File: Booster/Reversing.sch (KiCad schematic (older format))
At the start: 21 parts

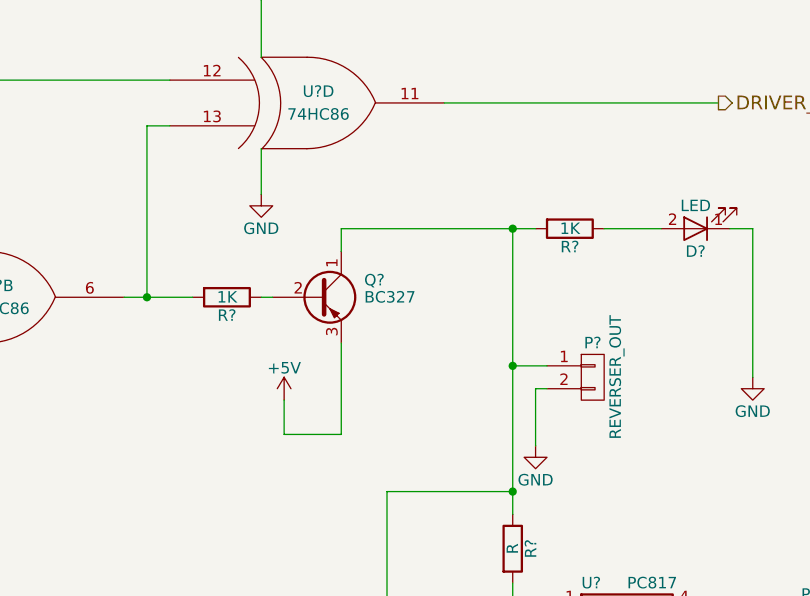
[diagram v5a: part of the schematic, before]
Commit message: Changed transistor driving reversing indicator LED to NPN to get it to light up when reversing, not light up when not reversing.
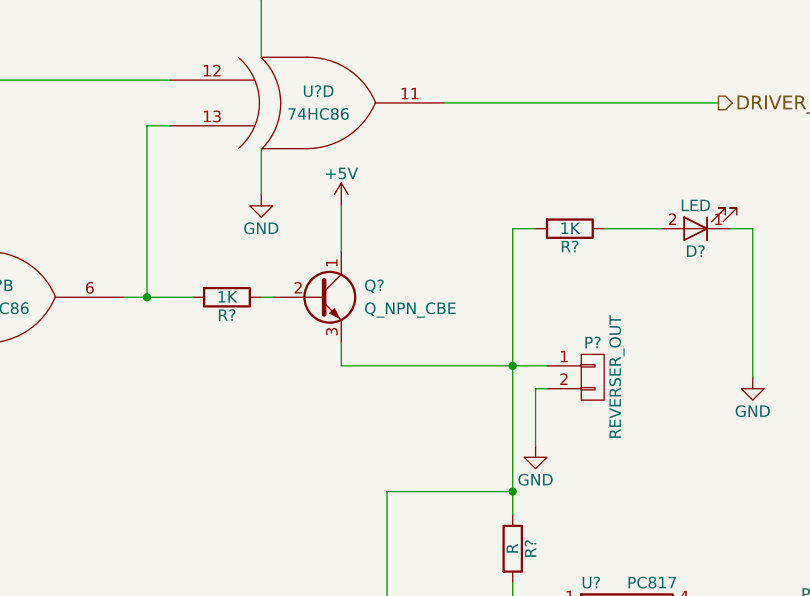
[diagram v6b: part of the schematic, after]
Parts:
- removed Q?: BC327, TO_SOT_Packages_THT:TO-92_Molded_Narrow, symbol BC327
- added Q?: Q_NPN_CBE, symbol Q_NPN_CBE
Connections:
- net +5V: now also Q?.1 (C)
- net at R?.1: now also Q?.2 (B)
- net at P?.1 (P1), R?.1, R?.1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: now also Q?.3 (E)
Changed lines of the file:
@@
 L +5V #PWR?
 U 1 1 5A08AC26
-P 5350 3900
-F 0 "#PWR?" H 5350 3750 50  0001 C CNN
-F 1 "+5V" H 5350 4040 50  0000 C CNN
-F 2 "" H 5350 3900 50  0000 C CNN
-F 3 "" H 5350 3900 50  0000 C CNN
-	1    5350 3900
+P 5600 3050
+F 0 "#PWR?" H 5600 2900 50  0001 C CNN
+F 1 "+5V" H 5600 3190 50  0000 C CNN
+F 2 "" H 5600 3050 50  0000 C CNN
+F 3 "" H 5600 3050 50  0000 C CNN
+	1    5600 3050
 	1    0    0    -1
 $EndComp
@@
 Wire Wire Line
 	6500 3850 6450 3850
-Connection ~ 6350 3150
-Wire Wire Line
-	6350 3750 6500 3750
+Wire Wire Line
+	5600 3750 6500 3750
 Wire Wire Line
 	6350 3150 6350 4400
 Wire Wire Line
-	5350 4050 5350 3900
-Wire Wire Line
-	5600 4050 5350 4050
-Wire Wire Line
-	5600 3650 5600 4050
-Wire Wire Line
 	7400 3150 7400 3800
 Wire Wire Line
@@
 	6750 3150 7000 3150
 Wire Wire Line
-	5600 3150 6450 3150
-Wire Wire Line
-	5600 3250 5600 3150
+	5600 3050 5600 3250
 Wire Wire Line
 	5250 3450 5300 3450
@@
 $EndComp
 $Comp
-L BC327 Q?
-U 1 1 5A1A0226
+L Q_NPN_CBE Q?
+U 1 1 5A3820E4
 P 5500 3450
-F 0 "Q?" H 5700 3525 50  0000 L CNN
-F 1 "BC327" H 5700 3450 50  0000 L CNN
-F 2 "TO_SOT_Packages_THT:TO-92_Molded_Narrow" H 5700 3375 50  0001 L CIN
-F 3 "" H 5500 3450 50  0001 L CNN
+F 0 "Q?" H 5700 3500 50  0000 L CNN
+F 1 "Q_NPN_CBE" H 5700 3400 50  0000 L CNN
+F 2 "" H 5700 3550 50  0000 C CNN
+F 3 "" H 5500 3450 50  0000 C CNN
 	1    5500 3450
 	1    0    0    -1
 $EndComp
+Wire Wire Line
+	6350 3150 6450 3150
+Wire Wire Line
+	5600 3750 5600 3650
 $EndSCHEMATC

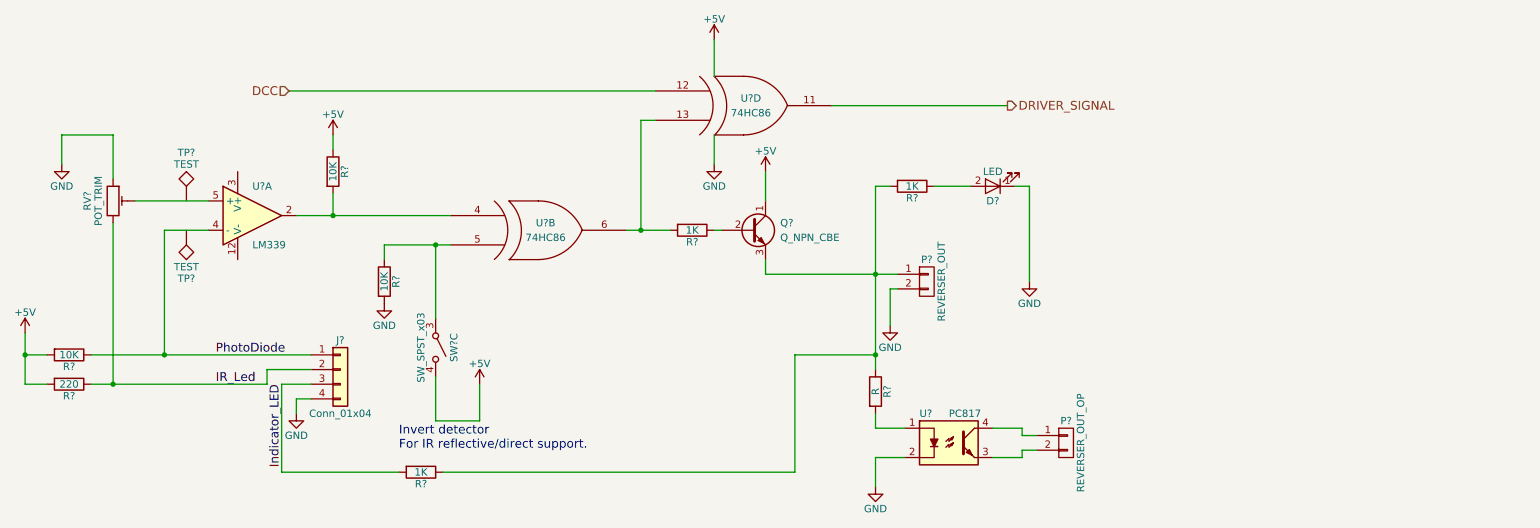
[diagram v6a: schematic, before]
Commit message: Removed need for enable signal replacing it with a missing pulse detection RC based circuit.
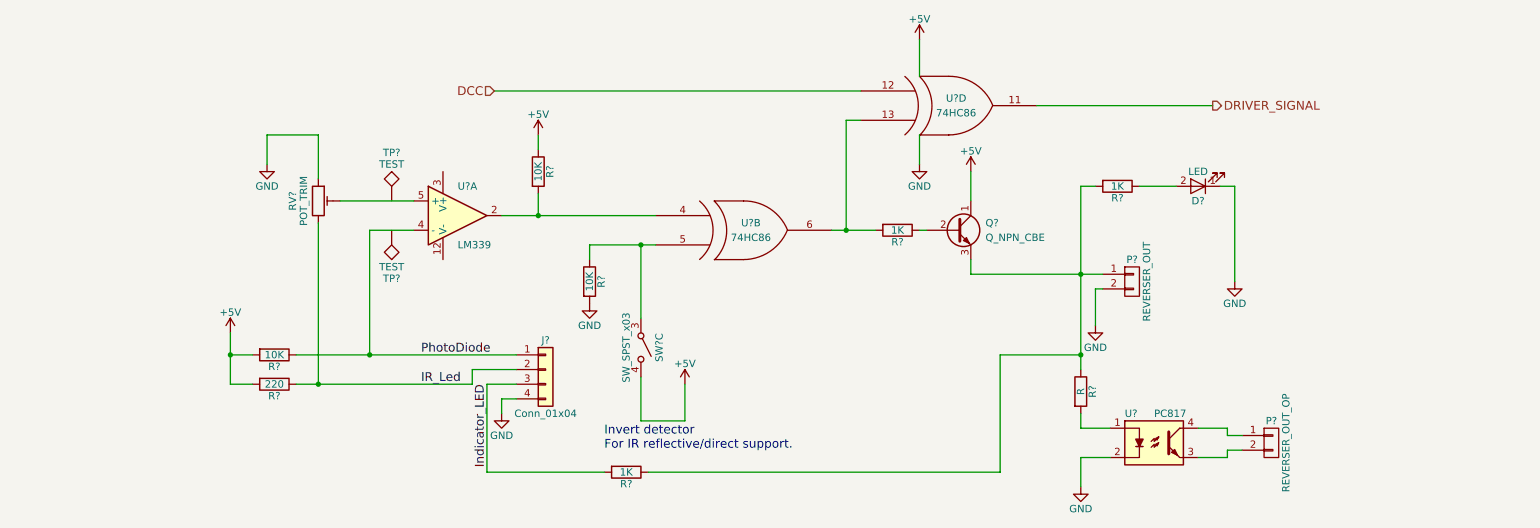
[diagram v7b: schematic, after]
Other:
- moved on the sheet: D?, J?, P?, Q?, R?, RV?, SW?C, TP?, U?, U?A, U?B, U?D

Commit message: Using spare xor gate to make all transistors PNP types.
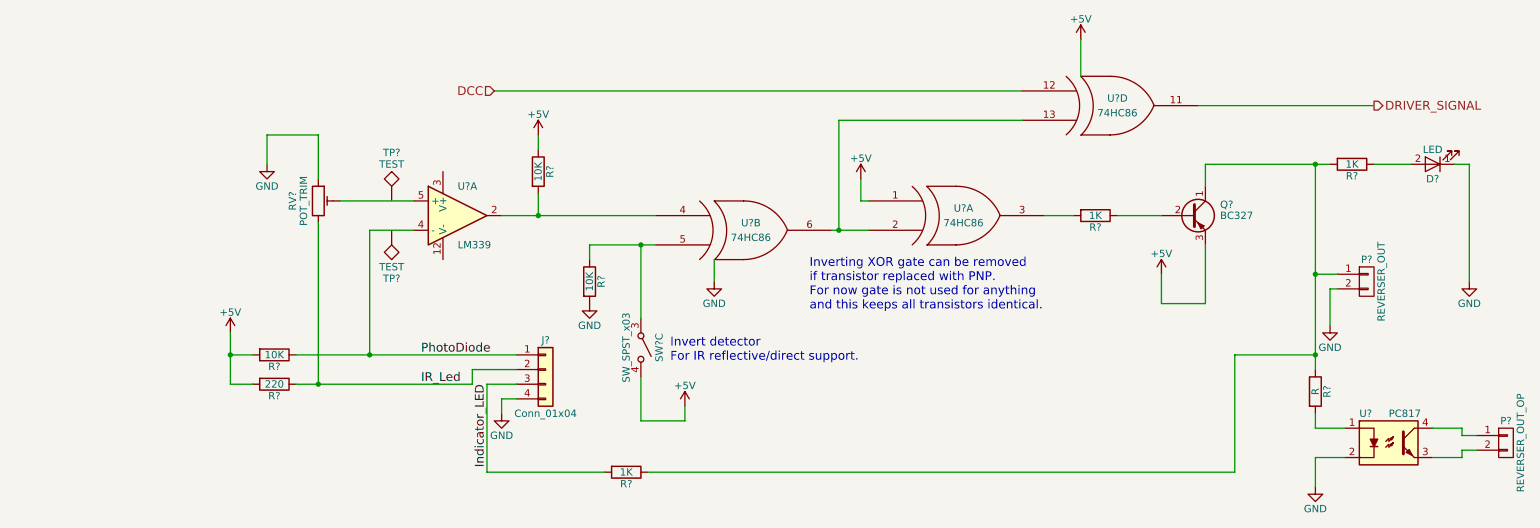
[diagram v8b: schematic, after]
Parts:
- removed Q?: Q_NPN_CBE, symbol Q_NPN_CBE
- added Q?: BC327, TO_SOT_Packages_THT:TO-92_Molded_Narrow, symbol BC327
- added U?: 74HC86, symbol 74LS86
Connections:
- net +5V: now also Q?.3 (E), U?.1 (IN1), U?.14 (VCC)
- net GND: now also U?.7 (GND)
- net at U?.13 (IN2), U?.6 (OUT): now also U?.2 (IN2); no longer R?.2
- net at R?.1: now also Q?.2 (B)
- net at P?.1 (P1), R?.1, R?.1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: now also Q?.1 (C)
- new net: R?.2, U?.3 (OUT)
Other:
- note added: "Inverting XOR gate can be removed\nif transistor replaced with PNP.\nFor now gate is not used for anything\nand this keeps all transistors identical."
- moved on the sheet: D?, P?, R?, U?, U?D
